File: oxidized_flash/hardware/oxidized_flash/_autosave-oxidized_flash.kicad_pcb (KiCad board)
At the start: 2 copper layers, 36 parts, among them J1 USB_B_Micro, U1 LM1117-3.3, U2 ATSAMD51G18A-MU, U3 IS21ES, Y1 32.768

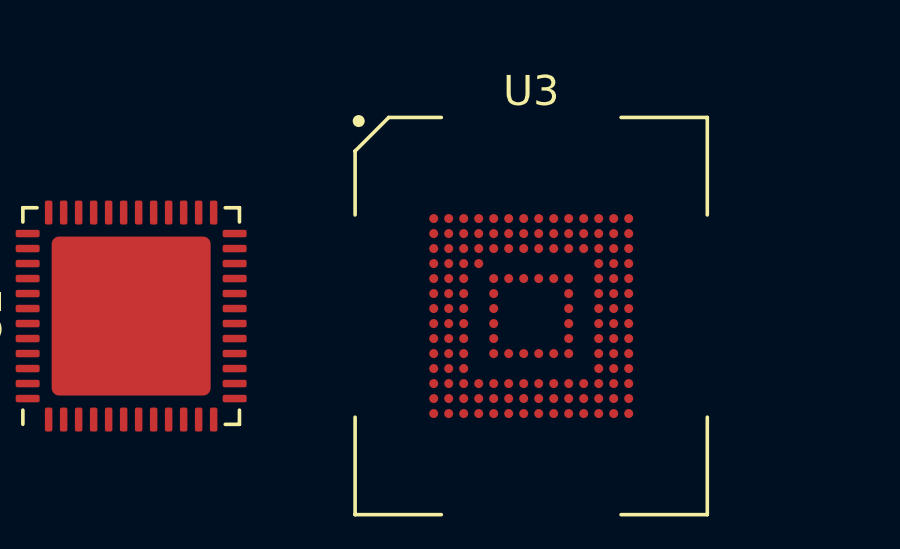
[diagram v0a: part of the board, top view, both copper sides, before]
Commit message: Add initial schematic, and SWD interface
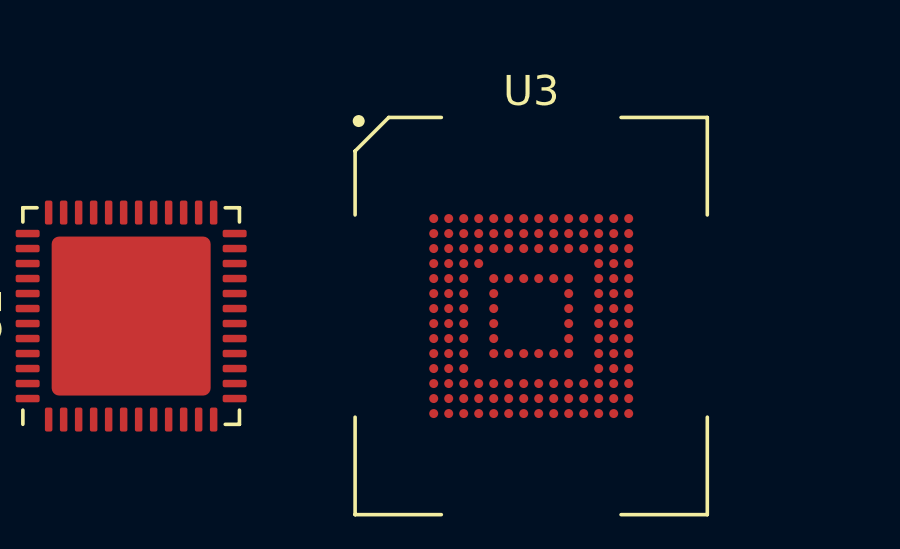
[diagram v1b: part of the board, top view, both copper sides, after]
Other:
- net class Default: clearance 0.2 -> 0.25
- rule pad_to_mask_clearance: 0.051 -> 0.05
- rule trace_clearance: 0.2 -> 0.25
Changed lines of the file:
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@@
     (thickness 1.6)
     (drawings 4)
-    (tracks 0)
+    (tracks 1)
     (zones 0)
     (modules 36)
@@
     (user_trace_width 0.0889)
     (user_trace_width 0.127)
-    (trace_clearance 0.2)
+    (trace_clearance 0.25)
     (zone_clearance 0.508)
     (zone_45_only no)
@@
     (pad_size 1.524 1.524)
     (pad_drill 0.762)
-    (pad_to_mask_clearance 0.051)
+    (pad_to_mask_clearance 0.05)
     (solder_mask_min_width 0.25)
     (aux_axis_origin 0 0)
-    (visible_elements FFFFFF7F)
+    (visible_elements FFFFEF7F)
     (pcbplotparams
       (layerselection 0x010fc_ffffffff)
@@
   (net 56 "Net-(U3-PadB6)")
   (net_class Default "This is the default net class."
-    (clearance 0.2)
+    (clearance 0.25)
     (trace_width 0.25)
     (via_dia 0.8)
@@
   (gr_line (start 31.75 31.75) (end 117.35 31.75) (layer Dwgs.User) (width 0.15))
   (gr_line (start 31.75 31.745) (end 31.75 85.725) (layer Dwgs.User) (width 0.15))
+  (segment (start 68.37 55.67) (end 68.456499 55.67) (width 0.127) (layer F.Cu) (net 25))
 )
